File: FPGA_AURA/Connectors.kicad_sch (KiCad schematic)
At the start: 2 parts, among them J1 SS5-40-3.00-X-D-K-XX, J2 SS5-20-3.00-X-D-K-XX

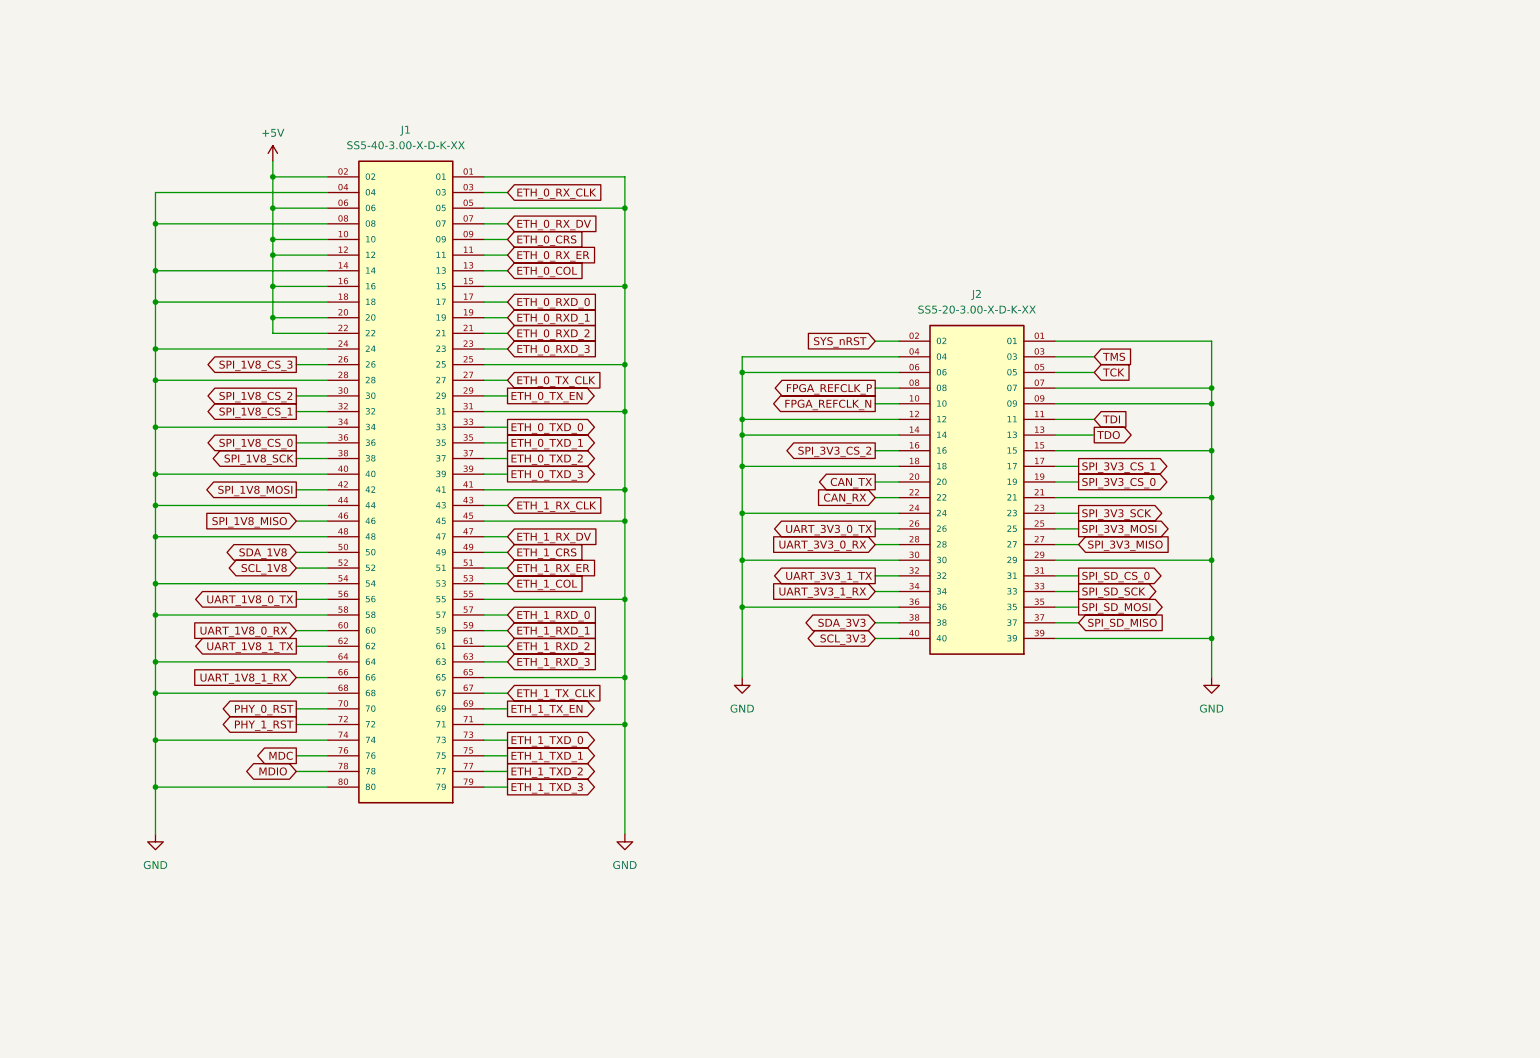
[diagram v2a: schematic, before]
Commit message: Finished schematic to start routing again, and started MII fanout from connector.
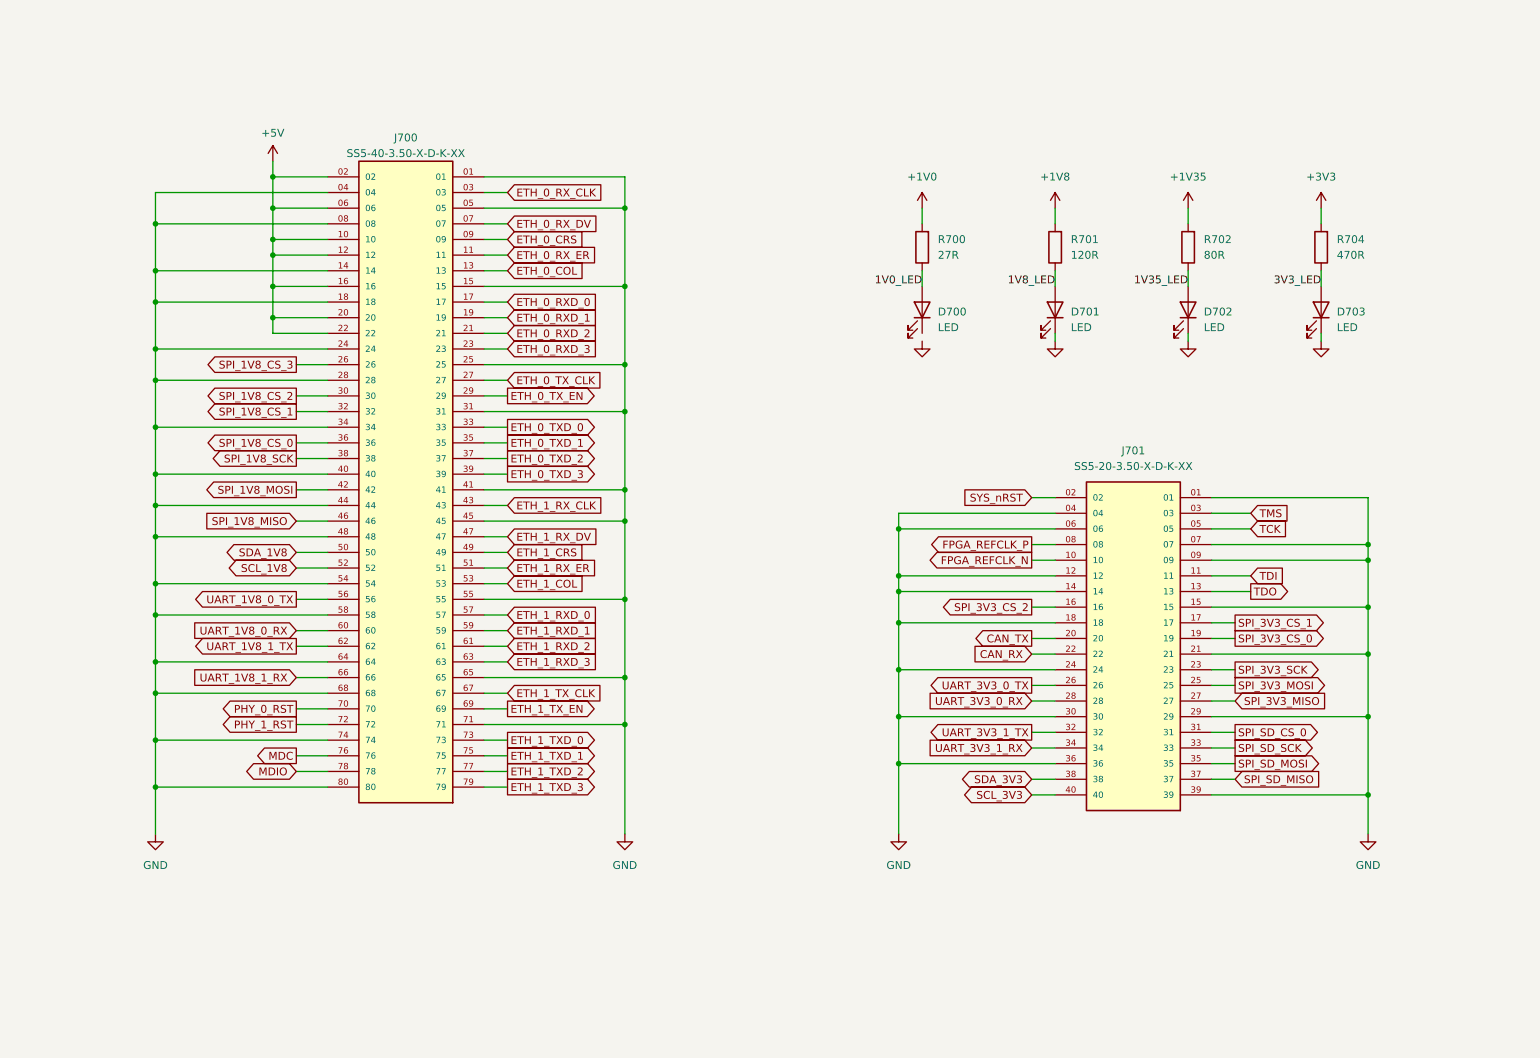
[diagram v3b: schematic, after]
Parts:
- removed J1: SS5-40-3.00-X-D-K-XX, SS5-40-3.00-X-D-K-XX:SAMTEC_SS5-40-3.00-X-D-K-XX, symbol SS5-40-3.00-X-D-K-XX:SS5-40-3.00-X-D-K-XX
- removed J2: SS5-20-3.00-X-D-K-XX, SS5-20-3.00-X-D-K-XX:SAMTEC_SS5-20-3.00-X-D-K-XX, symbol SS5-20-3.00-X-D-K-XX:SS5-20-3.00-X-D-K-XX
- added D700, D701, D702, D703: LED, LED_SMD:LED_0603_1608Metric, symbol Device:LED
- added J700: SS5-40-3.50-X-D-K-XX, SS5-40-3.50-X-D-K-XX:SAMTEC_SS5-40-3.50-X-D-K-XX, symbol SS5-40-3.50-X-D-K-XX:SS5-40-3.50-X-D-K-XX
- added J701: SS5-20-3.50-X-D-K-XX, SS5-20-3.50-X-D-K-XX:SAMTEC_SS5-20-3.50-X-D-K-XX, symbol SS5-20-3.50-X-D-K-XX:SS5-20-3.50-X-D-K-XX
- added R700: 27R, Resistor_SMD:R_0402_1005Metric, symbol Device:R
- added R701: 120R, Resistor_SMD:R_0402_1005Metric, symbol Device:R
- added R702: 80R, Resistor_SMD:R_0402_1005Metric, symbol Device:R
- added R704: 470R, Resistor_SMD:R_0402_1005Metric, symbol Device:R
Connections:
- net +5V: now also J700.02, J700.06, J700.10, J700.12, J700.16, J700.20, J700.22
- net CAN_RX: now also J701.22
- net CAN_TX: now also J701.20
- net ETH_0_COL: now also J700.13
- net ETH_0_CRS: now also J700.09
- net ETH_0_RXD_0: now also J700.17
- net ETH_0_RXD_1: now also J700.19
- net ETH_0_RXD_2: now also J700.21
- net ETH_0_RXD_3: now also J700.23
- net ETH_0_RX_CLK: now also J700.03
- net ETH_0_RX_DV: now also J700.07
- net ETH_0_RX_ER: now also J700.11
- net ETH_0_TXD_0: now also J700.33
- net ETH_0_TXD_1: now also J700.35
- net ETH_0_TXD_2: now also J700.37
- net ETH_0_TXD_3: now also J700.39
- net ETH_0_TX_CLK: now also J700.27
- net ETH_0_TX_EN: now also J700.29
- net ETH_1_COL: now also J700.53
- net ETH_1_CRS: now also J700.49
- net ETH_1_RXD_0: now also J700.57
- net ETH_1_RXD_1: now also J700.59
- net ETH_1_RXD_2: now also J700.61
- net ETH_1_RXD_3: now also J700.63
- net ETH_1_RX_CLK: now also J700.43
- net ETH_1_RX_DV: now also J700.47
- net ETH_1_RX_ER: now also J700.51
- net ETH_1_TXD_0: now also J700.73
- net ETH_1_TXD_1: now also J700.75
- net ETH_1_TXD_2: now also J700.77
- net ETH_1_TXD_3: now also J700.79
- net ETH_1_TX_CLK: now also J700.67
- net ETH_1_TX_EN: now also J700.69
- net FPGA_REFCLK_N: now also J701.10
- net FPGA_REFCLK_P: now also J701.08
- net GND: now also D701.1 (K), D702.1 (K), D703.1 (K), J700.01, J700.04, J700.05, J700.08, J700.14, J700.15, J700.18, J700.24, J700.25, J700.28, J700.31, J700.34, J700.40, J700.41, J700.44, J700.45, J700.48, J700.54, J700.55, J700.58, J700.64, J700.65, J700.68, J700.71, J700.74, J700.80, J701.01, J701.04, J701.06, J701.07, J701.09, J701.12, J701.14, J701.15, J701.18, J701.21, J701.24, J701.29, J701.30, J701.36, J701.39
- net MDC: now also J700.76
- net MDIO: now also J700.78
- net PHY_0_RST: now also J700.70
- net PHY_1_RST: now also J700.72
- net SCL_1V8: now also J700.52
- net SCL_3V3: now also J701.40
- net SDA_1V8: now also J700.50
- net SDA_3V3: now also J701.38
- net SPI_1V8_CS_0: now also J700.36
- net SPI_1V8_CS_1: now also J700.32
- net SPI_1V8_CS_2: now also J700.30
- net SPI_1V8_CS_3: now also J700.26
- net SPI_1V8_MISO: now also J700.46
- net SPI_1V8_MOSI: now also J700.42
- net SPI_1V8_SCK: now also J700.38
- net SPI_3V3_CS_0: now also J701.19
- net SPI_3V3_CS_1: now also J701.17
- net SPI_3V3_CS_2: now also J701.16
- net SPI_3V3_MISO: now also J701.27
- net SPI_3V3_MOSI: now also J701.25
- net SPI_3V3_SCK: now also J701.23
- net SPI_SD_CS_0: now also J701.31
- net SPI_SD_MISO: now also J701.37
- net SPI_SD_MOSI: now also J701.35
- net SPI_SD_SCK: now also J701.33
- net SYS_nRST: now also J701.02
- net TCK: now also J701.05
- net TDI: now also J701.11
- net TDO: now also J701.13
- net TMS: now also J701.03
- net UART_1V8_0_RX: now also J700.60
- net UART_1V8_0_TX: now also J700.56
- net UART_1V8_1_RX: now also J700.66
- net UART_1V8_1_TX: now also J700.62
- net UART_3V3_0_RX: now also J701.28
- net UART_3V3_0_TX: now also J701.26
- net UART_3V3_1_RX: now also J701.34
- net UART_3V3_1_TX: now also J701.32
- new net +1V0: R700.2
- new net +1V35: R702.2
- new net +1V8: R701.2
- new net +3V3: R704.2
- new net 1V0_LED: D700.2 (A), R700.1
- new net 1V35_LED: D702.2 (A), R702.1
- new net 1V8_LED: D701.2 (A), R701.1
- new net 3V3_LED: D703.2 (A), R704.1
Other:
- company: (none) -> Alexander Armitage
- title: (none) -> Connectors

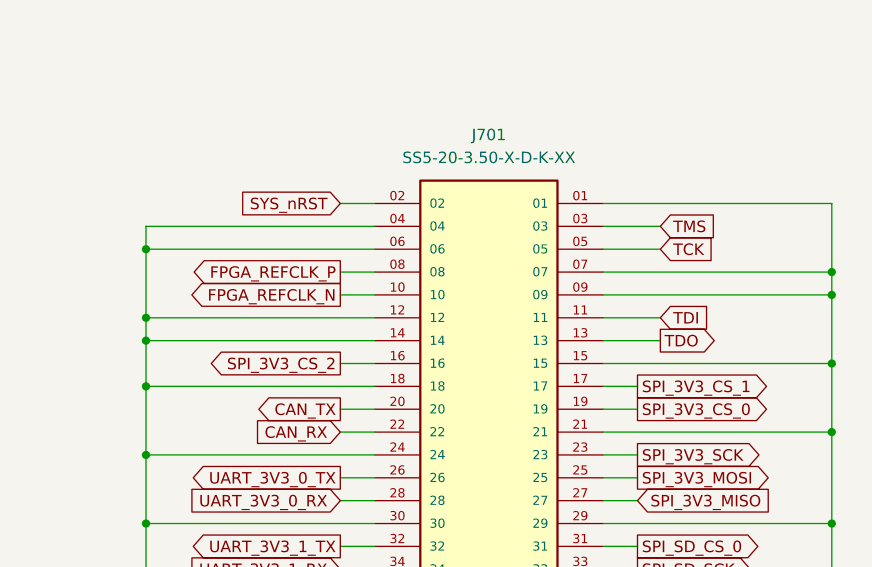
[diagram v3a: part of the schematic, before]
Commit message: All connector pins broken out. Next is QSPI flash, followed by power.
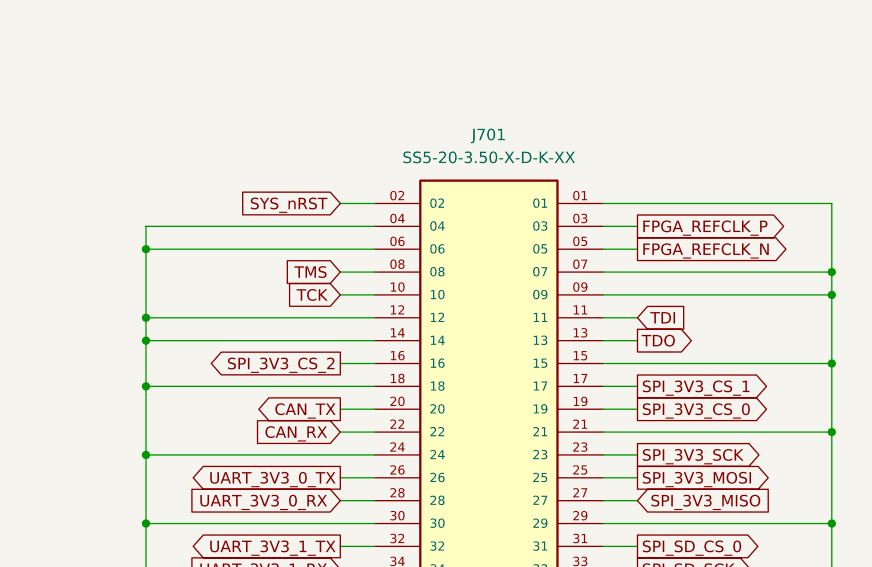
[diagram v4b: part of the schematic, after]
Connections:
- net FPGA_REFCLK_N: now also J701.05; no longer J701.10
- net FPGA_REFCLK_P: now also J701.03; no longer J701.08
- net TCK: now also J701.10; no longer J701.05
- net TMS: now also J701.08; no longer J701.03
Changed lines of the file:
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@@
 	(wire
 		(pts
-			(xy 228.6 100.33) (xy 234.95 100.33)
-		)
-		(stroke
-			(width 0)
-			(type default)
-		)
-	)
-	(wire
-		(pts
 			(xy 177.8 113.03) (xy 203.2 113.03)
 		)
@@
 	(wire
 		(pts
-			(xy 199.39 105.41) (xy 203.2 105.41)
-		)
-		(stroke
-			(width 0)
-			(type default)
-		)
-	)
-	(wire
-		(pts
 			(xy 110.49 68.58) (xy 114.3 68.58)
 		)
@@
 	(wire
 		(pts
+			(xy 199.39 105.41) (xy 203.2 105.41)
+		)
+		(stroke
+			(width 0)
+			(type default)
+		)
+	)
+	(wire
+		(pts
 			(xy 110.49 93.98) (xy 114.3 93.98)
 		)
@@
 	(wire
 		(pts
-			(xy 228.6 110.49) (xy 234.95 110.49)
+			(xy 228.6 110.49) (xy 232.41 110.49)
 		)
 		(stroke
@@
 	(wire
 		(pts
-			(xy 228.6 113.03) (xy 234.95 113.03)
+			(xy 228.6 113.03) (xy 232.41 113.03)
 		)
 		(stroke
@@
 	(wire
 		(pts
+			(xy 199.39 107.95) (xy 203.2 107.95)
+		)
+		(stroke
+			(width 0)
+			(type default)
+		)
+	)
+	(wire
+		(pts
 			(xy 80.01 91.44) (xy 85.09 91.44)
 		)
@@
 	(wire
 		(pts
+			(xy 228.6 100.33) (xy 232.41 100.33)
+		)
+		(stroke
+			(width 0)
+			(type default)
+		)
+	)
+	(wire
+		(pts
 			(xy 85.09 73.66) (xy 57.15 73.66)
 		)
@@
 	(wire
 		(pts
-			(xy 228.6 102.87) (xy 234.95 102.87)
+			(xy 228.6 102.87) (xy 232.41 102.87)
 		)
 		(stroke
@@
 	(wire
 		(pts
-			(xy 199.39 107.95) (xy 203.2 107.95)
-		)
-		(stroke
-			(width 0)
-			(type default)
-		)
-	)
-	(wire
-		(pts
 			(xy 57.15 144.78) (xy 85.09 144.78)
 		)
@@
 	(global_label "TCK"
 		(shape input)
-		(at 234.95 102.87 0)
+		(at 199.39 107.95 180)
 		(fields_autoplaced yes)
 		(effects
@@
 				(size 1.27 1.27)
 			)
-			(justify left)
+			(justify right)
 		)
 		(property "Intersheetrefs" "${INTERSHEET_REFS}"
-			(at 241.4428 102.87 0)
+			(at 192.8972 107.95 0)
 			(hide yes)
 			(show_name no)
@@
 					(size 1.27 1.27)
 				)
-				(justify left)
+				(justify right)
 			)
 		)
@@
 	(global_label "TDI"
 		(shape input)
-		(at 234.95 110.49 0)
+		(at 232.41 110.49 0)
 		(fields_autoplaced yes)
 		(effects
@@
 		)
 		(property "Intersheetrefs" "${INTERSHEET_REFS}"
-			(at 240.7776 110.49 0)
+			(at 238.2376 110.49 0)
 			(hide yes)
 			(show_name no)
@@
 	(global_label "TDO"
 		(shape output)
-		(at 234.95 113.03 0)
+		(at 232.41 113.03 0)
 		(fields_autoplaced yes)
 		(effects
@@
 		)
 		(property "Intersheetrefs" "${INTERSHEET_REFS}"
-			(at 241.5033 113.03 0)
+			(at 238.9633 113.03 0)
 			(hide yes)
 			(show_name no)
@@
 	(global_label "FPGA_REFCLK_N"
 		(shape output)
-		(at 199.39 107.95 180)
+		(at 232.41 102.87 0)
 		(fields_autoplaced yes)
 		(effects
@@
 				(size 1.27 1.27)
 			)
-			(justify right)
+			(justify left)
 		)
 		(property "Intersheetrefs" "${INTERSHEET_REFS}"
-			(at 181.3462 107.95 0)
+			(at 250.4538 102.87 0)
 			(hide yes)
 			(show_name no)
@@
 					(size 1.27 1.27)
 				)
-				(justify right)
+				(justify left)
 			)
 		)
@@
 	(global_label "FPGA_REFCLK_P"
 		(shape output)
-		(at 199.39 105.41 180)
+		(at 232.41 100.33 0)
 		(fields_autoplaced yes)
 		(effects
@@
 				(size 1.27 1.27)
 			)
-			(justify right)
+			(justify left)
 		)
 		(property "Intersheetrefs" "${INTERSHEET_REFS}"
-			(at 181.4067 105.41 0)
+			(at 250.3933 100.33 0)
 			(hide yes)
 			(show_name no)
@@
 					(size 1.27 1.27)
 				)
-				(justify right)
+				(justify left)
 			)
 		)
@@
 	(global_label "TMS"
 		(shape input)
-		(at 234.95 100.33 0)
+		(at 199.39 105.41 180)
 		(fields_autoplaced yes)
 		(effects
@@
 				(size 1.27 1.27)
 			)
-			(justify left)
+			(justify right)
 		)
 		(property "Intersheetrefs" "${INTERSHEET_REFS}"
-			(at 241.5637 100.33 0)
+			(at 192.7763 105.41 0)
 			(hide yes)
 			(show_name no)
@@
 					(size 1.27 1.27)
 				)
-				(justify left)
+				(justify right)
 			)
 		)

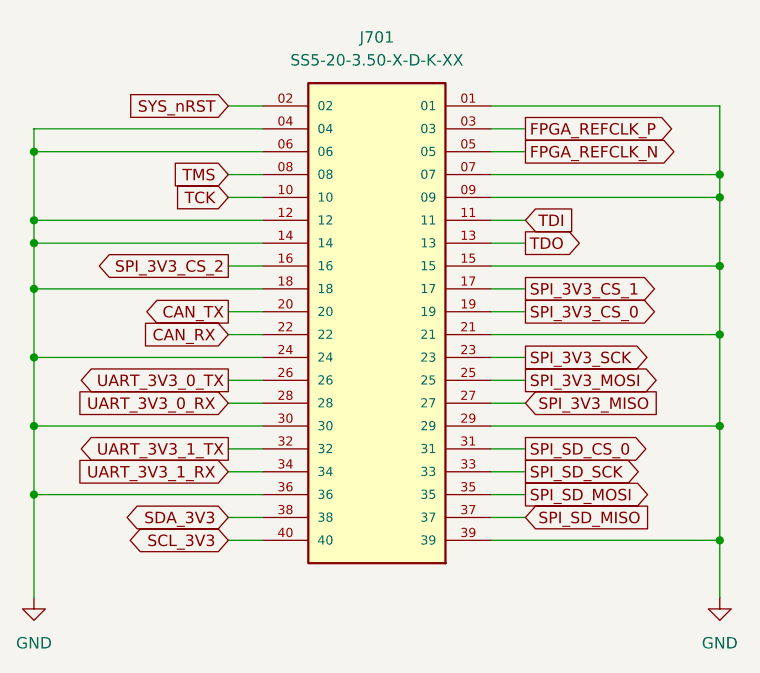
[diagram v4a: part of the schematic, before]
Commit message: Power planes done on layers 3 and 4 as well as almost all mezzanine connections made. QSPI and misc left to do.
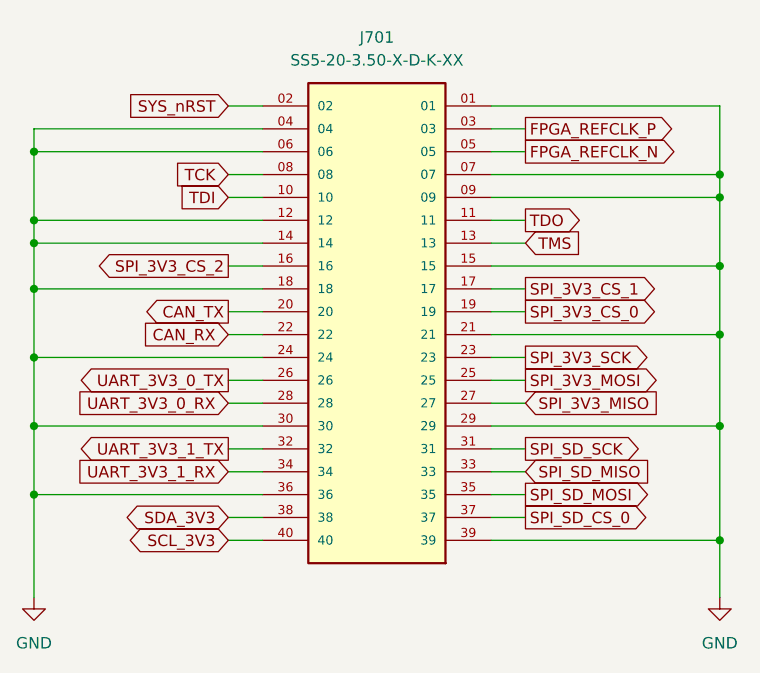
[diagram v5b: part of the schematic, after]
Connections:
- net SPI_SD_CS_0: now also J701.37; no longer J701.31
- net SPI_SD_MISO: now also J701.33; no longer J701.37
- net SPI_SD_SCK: now also J701.31; no longer J701.33
- net TCK: now also J701.08; no longer J701.10
- net TDI: now also J701.10; no longer J701.11
- net TDO: now also J701.11; no longer J701.13
- net TMS: now also J701.13; no longer J701.08
